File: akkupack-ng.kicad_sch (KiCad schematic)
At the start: 66 parts, among them J101 12V OUT, J102 36V IN, J103 36V OUT, J104 BAT, J105 OUT, J106 IN, J107 LED SW, J108 TEMP, Q101 2N7002, Q102 BSS84, Q103 2N7002, SW101 LED Enable, U101 BQ34Z100PWR-G1, U102 74HC164, U103 74HC164

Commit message: Update to KiCAD 9.x
Signed-off-by: Benedikt Spranger <b.spranger@linutronix.de>
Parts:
- U101: Description_1 (none) -> Multi-chemistry Impedance Track™ standalone fuel gauge | ba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
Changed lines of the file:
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@@
 (kicad_sch
-	(version 20231120)
+	(version 20250114)
 	(generator "eeschema")
-	(generator_version "8.0")
+	(generator_version "9.0")
 	(paper "A4")
 	(title_block
@@
 	(label "SDA"
 		(at 187.96 40.64 180)
-		(fields_autoplaced yes)
 		(effects
 			(font
@@
 	(label "P1"
 		(at 109.22 124.46 180)
-		(fields_autoplaced yes)
 		(effects
 			(font
@@
 	(label "BAT"
 		(at 96.52 55.88 180)
-		(fields_autoplaced yes)
 		(effects
 			(font
@@
 	(label "P1"
 		(at 96.52 66.04 180)
-		(fields_autoplaced yes)
 		(effects
 			(font
@@
 	(label "SDA"
 		(at 96.52 71.12 180)
-		(fields_autoplaced yes)
 		(effects
 			(font
@@
 	(label "~{ALERT}"
 		(at 187.96 45.72 180)
-		(fields_autoplaced yes)
 		(effects
 			(font
@@
 	(label "SCL"
 		(at 137.16 68.58 0)
-		(fields_autoplaced yes)
 		(effects
 			(font
@@
 	(label "SCL"
 		(at 187.96 43.18 180)
-		(fields_autoplaced yes)
 		(effects
 			(font
@@
 	(label "P2"
 		(at 96.52 68.58 180)
-		(fields_autoplaced yes)
 		(effects
 			(font
@@
 	(label "BAT"
 		(at 45.72 152.4 180)
-		(fields_autoplaced yes)
 		(effects
 			(font
@@
 	(label "~{ALERT}"
 		(at 137.16 71.12 0)
-		(fields_autoplaced yes)
 		(effects
 			(font
@@
 	(label "P2"
 		(at 109.22 132.08 180)
-		(fields_autoplaced yes)
 		(effects
 			(font
@@
 			)
 		)
+		(property "Sim.Pins" "1=K 2=A"
+			(at 177.8 100.33 0)
+			(effects
+				(font
+					(size 1.27 1.27)
+				)
+			)
+		)
 		(pin "2"
 		)
@@
 			)
 		)
+		(property "Sim.Pins" "1=K 2=A"
+			(at 266.7 100.33 0)
+			(effects
+				(font
+					(size 1.27 1.27)
+				)
+			)
+		)
 		(pin "2"
 		)
@@
 			)
 		)
+		(property "Sim.Pins" "1=K 2=A"
+			(at 190.5 100.33 0)
+			(effects
+				(font
+					(size 1.27 1.27)
+				)
+			)
+		)
 		(pin "2"
 		)
@@
 			)
 		)
+		(property "Sim.Pins" "1=K 2=A"
+			(at 203.2 100.33 0)
+			(effects
+				(font
+					(size 1.27 1.27)
+				)
+			)
+		)
 		(pin "2"
 		)
@@
 			)
 		)
+		(property "Sim.Pins" "1=K 2=A"
+			(at 241.3 100.33 0)
+			(effects
+				(font
+					(size 1.27 1.27)
+				)
+			)
+		)
 		(pin "2"
 		)
@@
 			)
 		)
+		(property "Sim.Pins" "1=K 2=A"
+			(at 215.9 100.33 0)
+			(effects
+				(font
+					(size 1.27 1.27)
+				)
+			)
+		)
 		(pin "2"
 		)
@@
 			)
 		)
+		(property "Sim.Enable" "0"
+			(at 278.13 160.02 0)
+			(effects
+				(font
+					(size 1.27 1.27)
+				)
+			)
+		)
 		(instances
 			(project "akkupack-ng"
@@
 			)
 		)
+		(property "Sim.Pins" "1=K 2=A"
+			(at 152.4 100.33 0)
+			(effects
+				(font
+					(size 1.27 1.27)
+				)
+			)
+		)
 		(pin "2"
 		)
@@
 			)
 		)
+		(property "Sim.Pins" "1=K 2=A"
+			(at 254 100.33 0)
+			(effects
+				(font
+					(size 1.27 1.27)
+				)
+			)
+		)
 		(pin "2"
 		)
@@
 			)
 		)
+		(property "Sim.Pins" "1=K 2=A"
+			(at 165.1 100.33 0)
+			(effects
+				(font
+					(size 1.27 1.27)
+				)
+			)
+		)
 		(pin "2"
 		)
@@
 			)
 		)
+		(property "Description_1" "\nMulti-chemistry Impedance Track™ standalone fuel gauge | battery gas gauge\n"
+			(at 116.84 73.66 0)
+			(effects
+				(font
+					(size 1.27 1.27)
+				)
+				(justify bottom)
+			)
+		)
 		(pin "7"
 		)
@@
 			)
 		)
+		(property "Sim.Pins" "1=K 2=A"
+			(at 228.6 100.33 0)
+			(effects
+				(font
+					(size 1.27 1.27)
+				)
+			)
+		)
 		(pin "2"
 		)
@@
 		(at 190.5 38.1)
 		(size 12.7 25.4)
+		(exclude_from_sim no)
+		(in_bom yes)
+		(on_board yes)
+		(dnp no)
 		(fields_autoplaced yes)
 		(stroke
@@
 		)
 	)
+	(embedded_fonts no)
 )

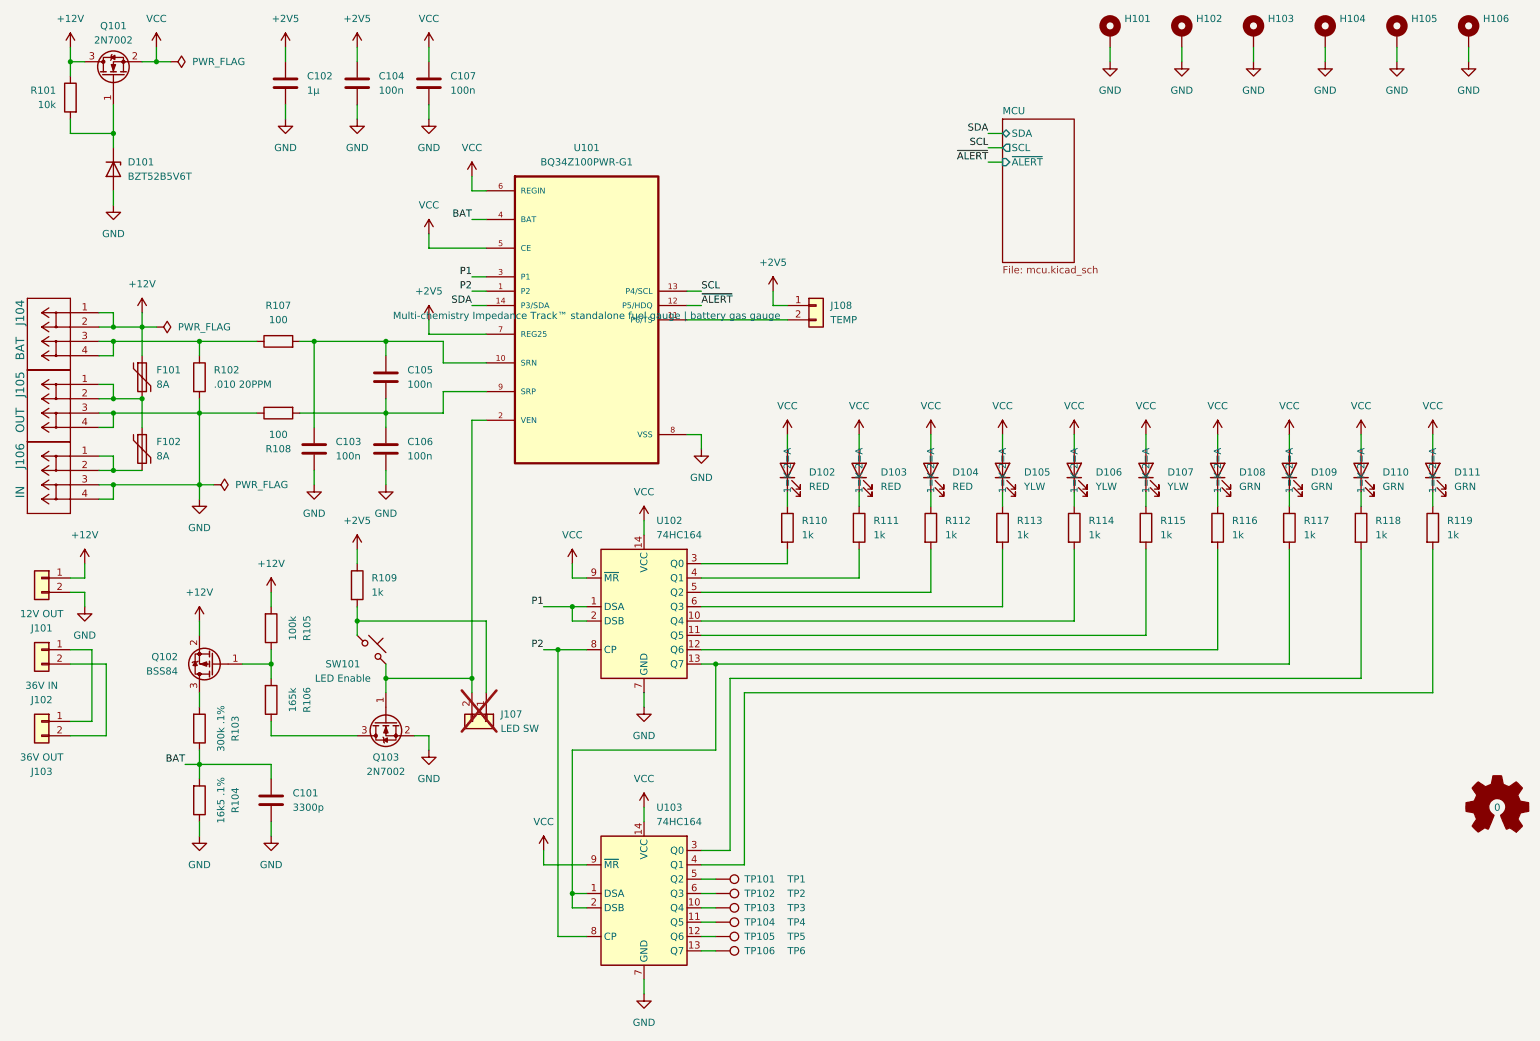
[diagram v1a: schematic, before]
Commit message: Rework Input selection
Signed-off-by: Benedikt Spranger <b.spranger@linutronix.de>
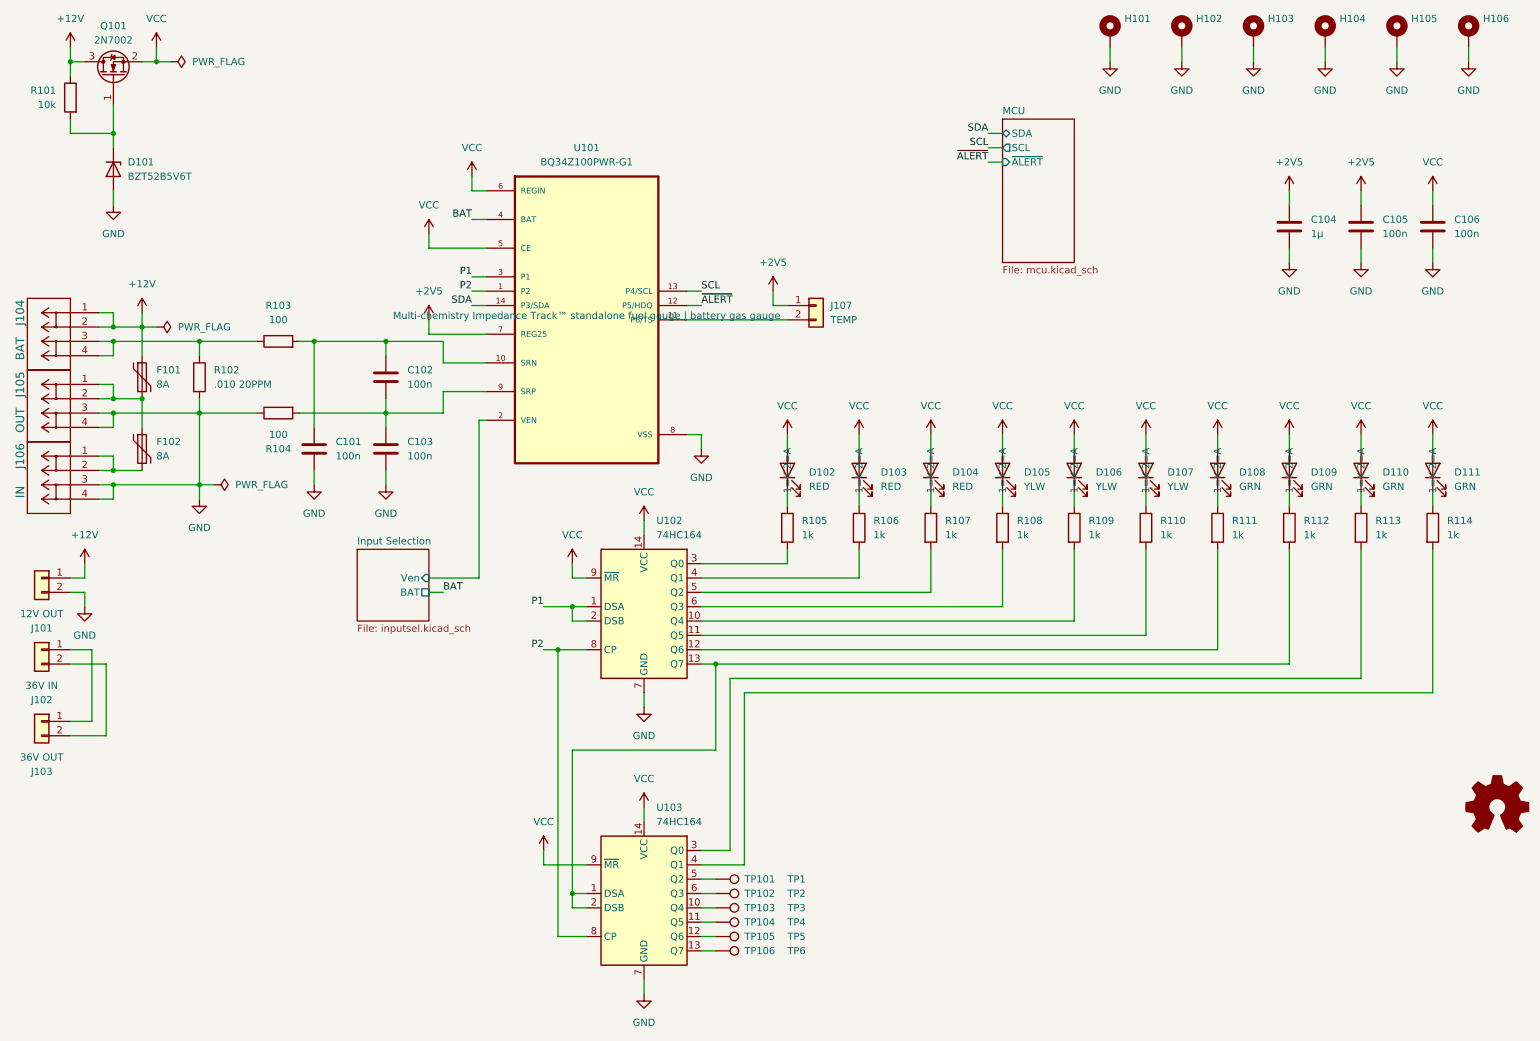
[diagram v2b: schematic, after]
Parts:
- removed C101: 3300p, Capacitor_SMD:C_1206_3216Metric, symbol Device:C
- removed J107: LED SW, Connector_JST:JST_XH_B2B-XH-A_1x02_P2.50mm_Vertical, symbol Connector_Generic:Conn_01x02
- removed Q102: BSS84, Package_TO_SOT_SMD:SOT-23, symbol Transistor_FET:BSS84
- removed Q103: 2N7002, Package_TO_SOT_SMD:SOT-23, symbol Transistor_FET:2N7002
- removed R103: 300k .1%, Resistor_SMD:R_0603_1608Metric, symbol Device:R
- removed R104: 16k5 .1%, Resistor_SMD:R_0603_1608Metric, symbol Device:R
- removed R105: 100k, Resistor_SMD:R_0402_1005Metric, symbol Device:R
- removed R106: 165k, Resistor_SMD:R_0402_1005Metric, symbol Device:R
- removed R109: 1k, Resistor_SMD:R_0402_1005Metric, symbol Device:R
- removed SW101: LED Enable, footprint:Push_SW_5x5, symbol Switch:SW_Push_45deg
- renumbered C103 to C101, C105 to C102, C106 to C103, C102 to C104, C104 to C105, C107 to C106, J108 to J107, R107 to R103, R108 to R104, R110 to R105, R111 to R106, R112 to R107, R113 to R108, R114 to R109, R115 to R110, R116 to R111, R117 to R112, R118 to R113, R119 to R114
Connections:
- net Input Selection/Ven: now reaches U101.2 (VEN)
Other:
- added sheet Input Selection (inputsel.kicad_sch)
- moved on the sheet: C104, C105, C106

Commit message: Available Parts
Signed-off-by: Benedikt Spranger <bene@eurovibes.org>
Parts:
- D101: MF LRC -> hongjiacheng; MP LBZT52B5V6T1G -> BZT52B5V6; SupplLink https://jlcpcb.com/partdetail/Lrc-LBZT52B5V6T1G/C2912016 -> https://jlcpcb.com/partdetail/Hongjiacheng-BZT52B5V6/C22399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; lcsc# C2912016 -> C22399881
- D102, D103, D104: Long Description 90mcd Red 615nm~630nm Upright, surface-mount Red 120° 75mW 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 -> -40℃~+85℃ Red 0603 LED Indication - Discrete ROHS; MF XINGLIGHT -> Hubei KENTO Elec; MP XL-1608VRC-06 -> KT-0603R; SupplLink https://jlcpcb.com/partdetail/Xinglight-XL_1608VRC06/C73719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 -> https://jlcpcb.com/partdetail/Hubei_KentoElec-KT0603R/C2286; lcsc# C7371906 -> C2286
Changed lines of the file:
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@@
 			)
 		)
-		(property "lcsc#" "C7371906"
+		(property "lcsc#" "C2286"
 			(at 177.8 100.33 0)
 			(effects
@@
 			)
 		)
-		(property "Long Description" "90mcd Red 615nm~630nm Upright, surface-mount Red 120° 75mW 0603 Light Emitting Diodes (LED) ROHS"
+		(property "Long Description" "-40℃~+85℃ Red 0603 LED Indication - Discrete ROHS"
 			(at 177.8 100.33 0)
 			(effects
@@
 			)
 		)
-		(property "SupplLink" "https://jlcpcb.com/partdetail/Xinglight-XL_1608VRC06/C7371906"
+		(property "SupplLink" "https://jlcpcb.com/partdetail/Hubei_KentoElec-KT0603R/C2286"
 			(at 177.8 100.33 0)
 			(effects
@@
 			)
 		)
-		(property "MF" "XINGLIGHT"
+		(property "MF" "Hubei KENTO Elec"
 			(at 177.8 100.33 0)
 			(effects
@@
 			)
 		)
-		(property "MP" "XL-1608VRC-06"
+		(property "MP" " KT-0603R"
 			(at 177.8 100.33 0)
 			(effects
@@
 			)
 		)
-		(property "lcsc#" "C2912016"
+		(property "lcsc#" "C22399881"
 			(at 33.02 46.99 0)
 			(effects
@@
 			)
 		)
-		(property "SupplLink" "https://jlcpcb.com/partdetail/Lrc-LBZT52B5V6T1G/C2912016"
+		(property "SupplLink" "https://jlcpcb.com/partdetail/Hongjiacheng-BZT52B5V6/C22399881"
 			(at 33.02 46.99 0)
 			(effects
@@
 			)
 		)
-		(property "MF" "LRC"
+		(property "MF" "hongjiacheng"
 			(at 33.02 46.99 0)
 			(effects
@@
 			)
 		)
-		(property "MP" "LBZT52B5V6T1G"
+		(property "MP" "BZT52B5V6"
 			(at 33.02 46.99 0)
 			(effects
@@
 			)
 		)
-		(property "lcsc#" "C7371906"
+		(property "lcsc#" "C2286"
 			(at 152.4 100.33 0)
 			(effects
@@
 			)
 		)
-		(property "Long Description" "90mcd Red 615nm~630nm Upright, surface-mount Red 120° 75mW 0603 Light Emitting Diodes (LED) ROHS"
+		(property "Long Description" "-40℃~+85℃ Red 0603 LED Indication - Discrete ROHS"
 			(at 152.4 100.33 0)
 			(effects
@@
 			)
 		)
-		(property "SupplLink" "https://jlcpcb.com/partdetail/Xinglight-XL_1608VRC06/C7371906"
+		(property "SupplLink" "https://jlcpcb.com/partdetail/Hubei_KentoElec-KT0603R/C2286"
 			(at 152.4 100.33 0)
 			(effects
@@
 			)
 		)
-		(property "MF" "XINGLIGHT"
+		(property "MF" "Hubei KENTO Elec"
 			(at 152.4 100.33 0)
 			(effects
@@
 			)
 		)
-		(property "MP" "XL-1608VRC-06"
+		(property "MP" " KT-0603R"
 			(at 152.4 100.33 0)
 			(effects
@@
 			)
 		)
-		(property "lcsc#" "C7371906"
+		(property "lcsc#" "C2286"
 			(at 165.1 100.33 0)
 			(effects
@@
 			)
 		)
-		(property "Long Description" "90mcd Red 615nm~630nm Upright, surface-mount Red 120° 75mW 0603 Light Emitting Diodes (LED) ROHS"
+		(property "Long Description" "-40℃~+85℃ Red 0603 LED Indication - Discrete ROHS"
 			(at 165.1 100.33 0)
 			(effects
@@
 			)
 		)
-		(property "SupplLink" "https://jlcpcb.com/partdetail/Xinglight-XL_1608VRC06/C7371906"
+		(property "SupplLink" "https://jlcpcb.com/partdetail/Hubei_KentoElec-KT0603R/C2286"
 			(at 165.1 100.33 0)
 			(effects
@@
 			)
 		)
-		(property "MF" "XINGLIGHT"
+		(property "MF" "Hubei KENTO Elec"
 			(at 165.1 100.33 0)
 			(effects
@@
 			)
 		)
-		(property "MP" "XL-1608VRC-06"
+		(property "MP" " KT-0603R"
 			(at 165.1 100.33 0)
 			(effects
